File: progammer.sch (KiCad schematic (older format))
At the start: 10 parts, among them J5 USB_B_Micro, U1 ICE40HX4K-TQ144, U3 93LCxxBT-I_OT, U4 FT2232H, U5 IS25LP080D

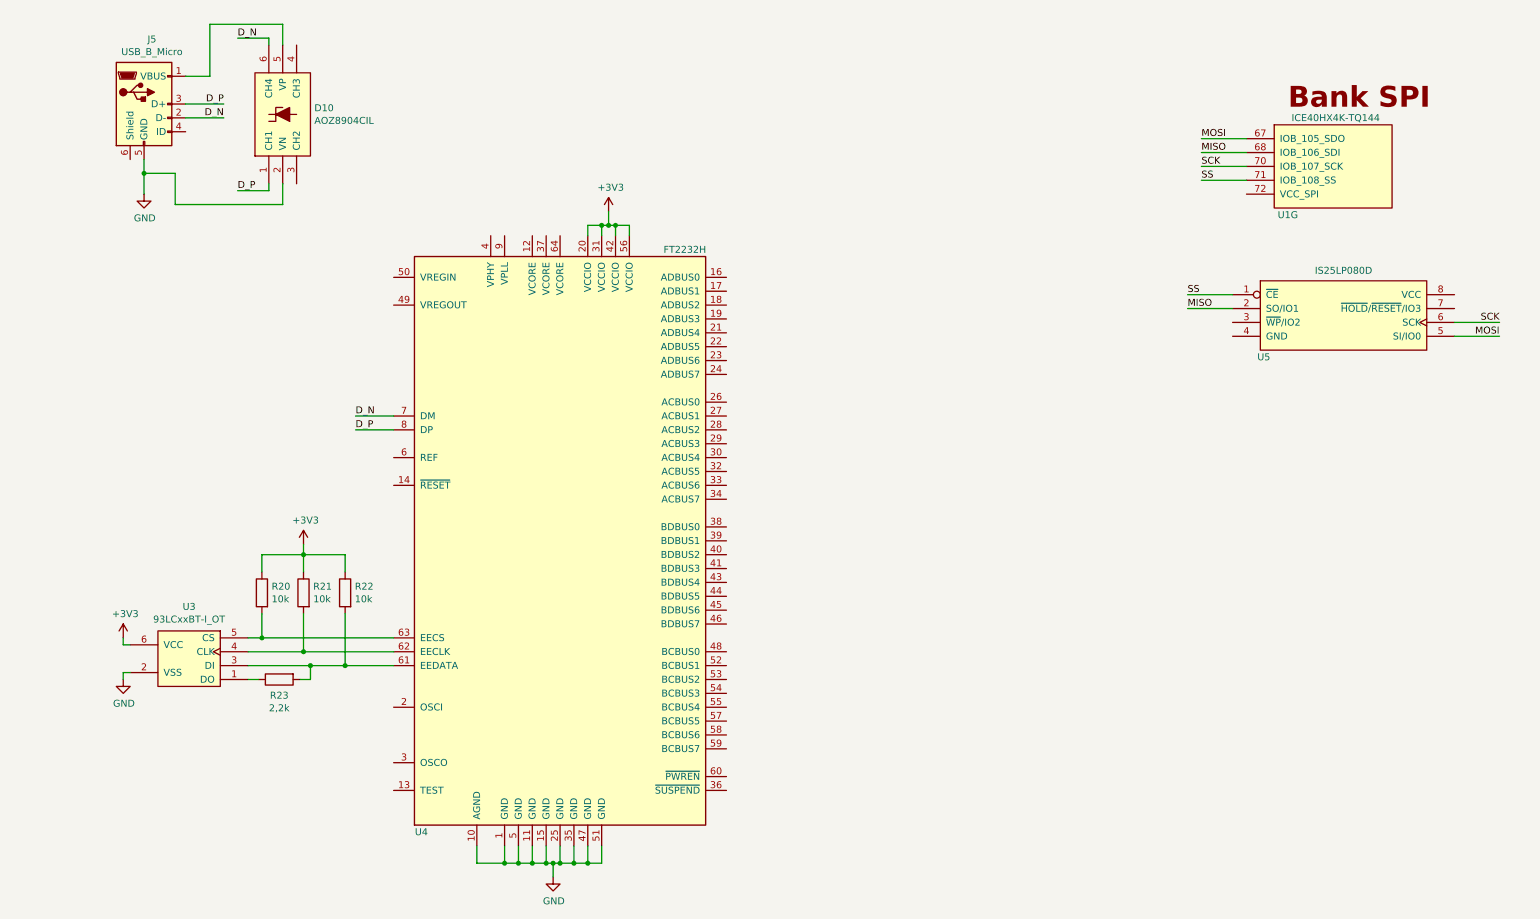
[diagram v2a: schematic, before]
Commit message: Progress on FTDI - added Oscillator and 1.8 V supply
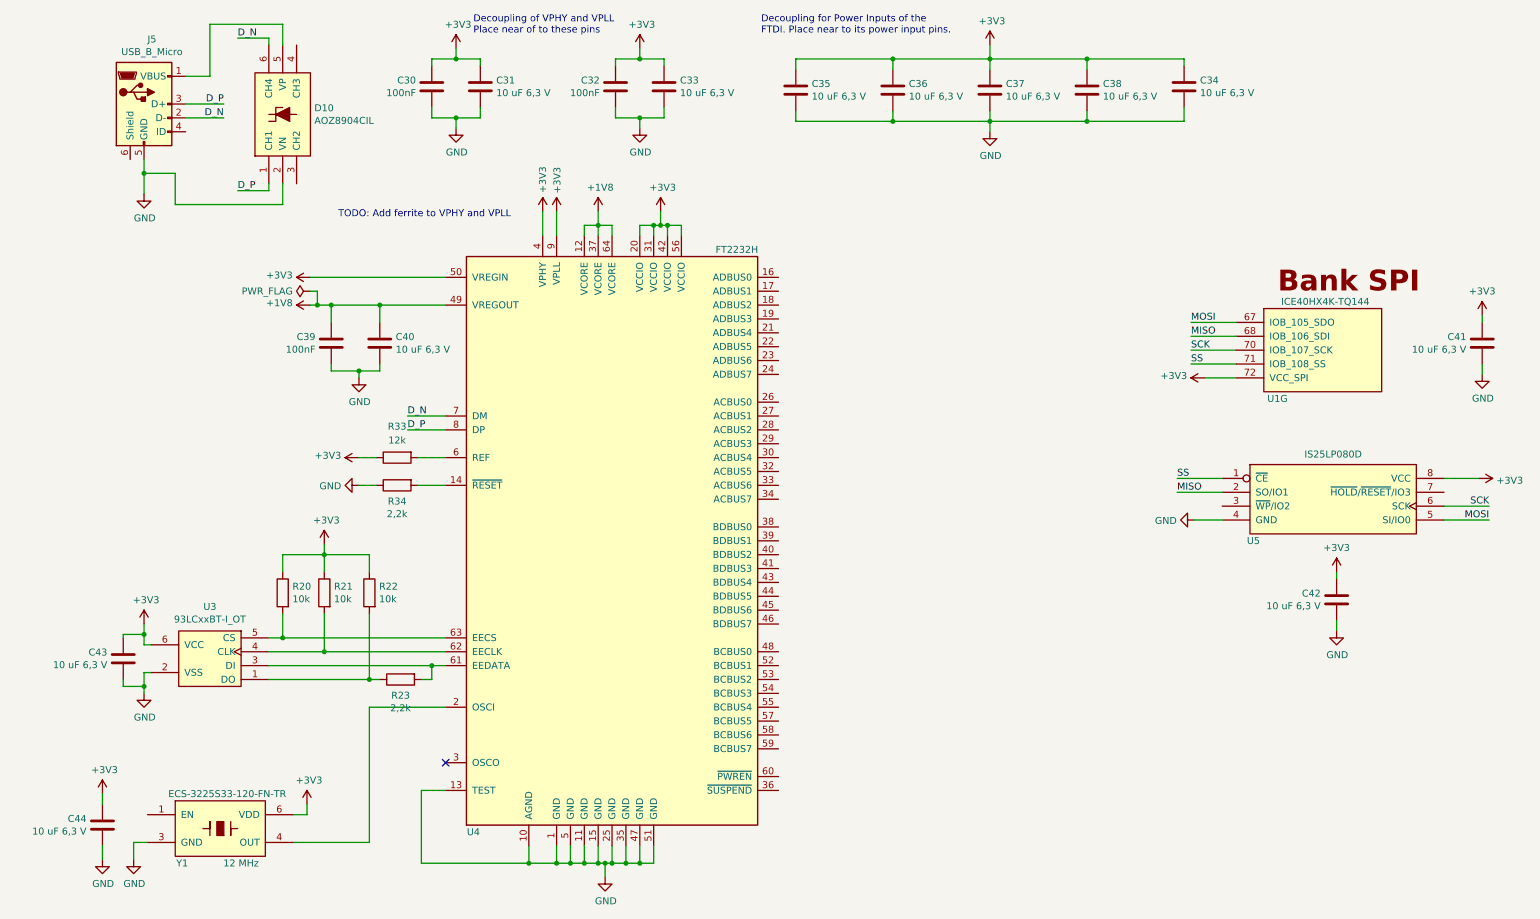
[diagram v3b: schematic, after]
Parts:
- added C30, C32, C39: 100nF, Capacitor_SMD:C_0603_1608Metric, symbol Device:C
- added C31, C33, C34, C35, C36, C37, C38, C40, C41, C42, C43, C44: 10 uF 6,3 V, Capacitor_SMD:C_0603_1608Metric, symbol Device:C
- added R33: 12k, Resistor_SMD:R_0603_1608Metric, symbol Device:R
- added R34: 2,2k, Resistor_SMD:R_0603_1608Metric, symbol Device:R
- added Y1: ECS-3225S33-120-FN-TR, footprints:ECS-3225S_3.2x2.5mm_footprint, symbol ECS-3225S:ECS-3225S33
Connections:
- net +3V3: now also U1.72 (VCC_SPI), U4.4 (VPHY), U4.50 (VREGIN), U4.9 (VPLL), U5.8 (VCC), C30.1, C31.1, C32.1, C33.1, C34.1, C35.1, C36.1, C37.1, C38.1, C41.1, C42.1, C43.1, C44.1, R33.1, Y1.6 (VDD)
- net GND: now also U4.13 (TEST), U5.4 (GND), C30.2, C31.2, C32.2, C33.2, C34.2, C35.2, C36.2, C37.2, C38.2, C39.2, C40.2, C41.2, C42.2, C43.2, C44.2, R34.1, Y1.3 (GND)
- net +1V8: now reaches U4.12 (VCORE)
- net +1V8: now also U4.37 (VCORE), U4.49 (VREGOUT), U4.64 (VCORE), C39.1, C40.1
- net at U4.14 (~RESET): now also R34.2
- net at U4.2 (OSCI): now also Y1.4 (OUT)
- net at U4.6 (REF): now also R33.2
- net at R23.2, U3.3 (DI), U4.61 (EEDATA): no longer R22.2
- net at R23.1, U3.1 (DO): now also R22.2
- no-connect marks 0 -> 1
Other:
- note added: "Decoupling for Power Inputs of the\nFTDI. Place near to its power input pins."
- note added: "Decoupling of VPHY and VPLL\nPlace near of to these pins"
- note added: "TODO: Add ferrite to VPHY and VPLL"
- moved on the sheet: R20, R21, R22, R23, U1G, U3, U4, U5

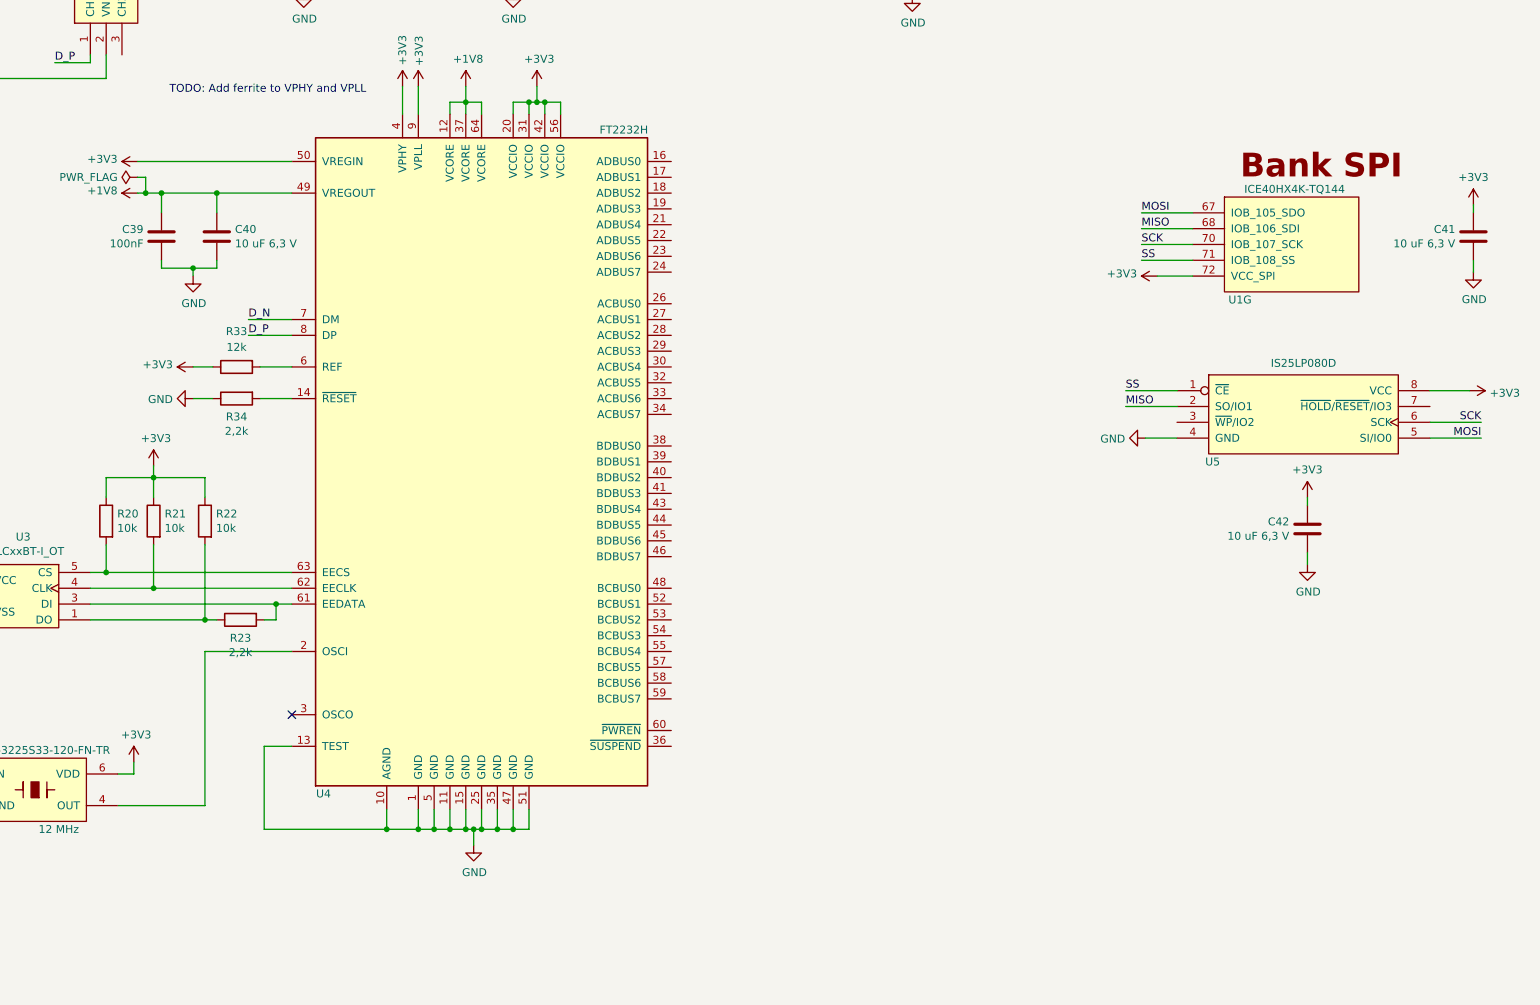
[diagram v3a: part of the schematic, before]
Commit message: Continued on Programmer, moved the header signals around the package to free some space for a fully featured UART/RS232(TTL)
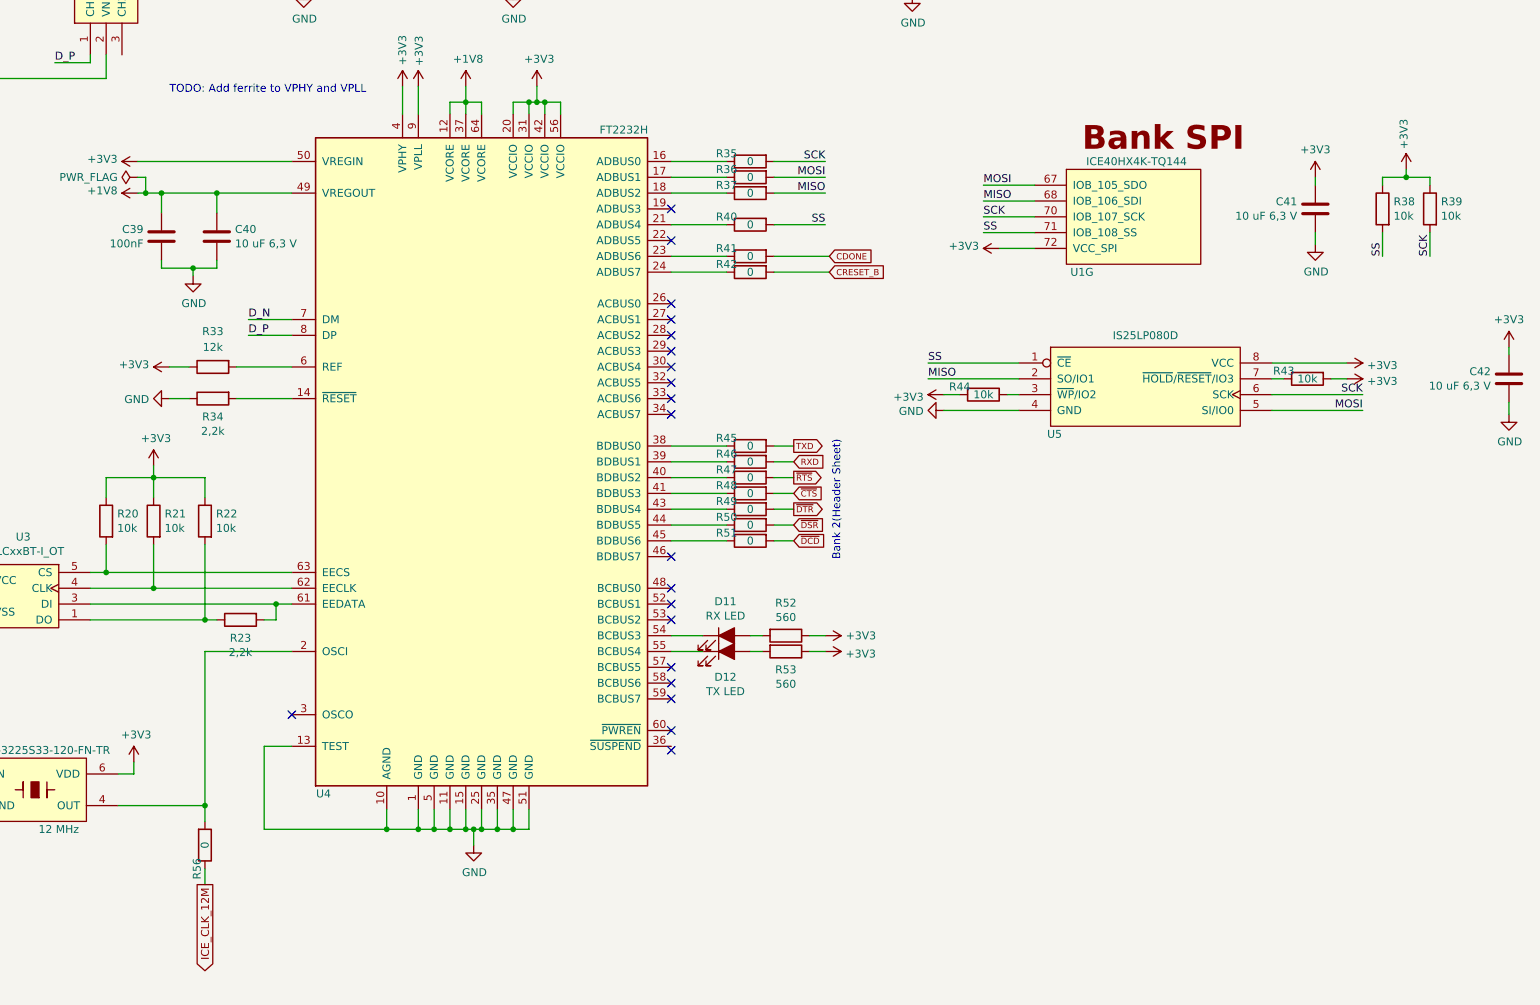
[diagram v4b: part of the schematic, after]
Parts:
- added D11: RX LED, LED_SMD:LED_0603_1608Metric, symbol Device:LED_ALT
- added D12: TX LED, LED_SMD:LED_0603_1608Metric, symbol Device:LED_ALT
- added R35, R36, R37, R40, R41, R42, R45, R46, R47, R48, R49, R50, R51, R56: 0, Resistor_SMD:R_0603_1608Metric, symbol Device:R
- added R38, R39, R43, R44: 10k, Resistor_SMD:R_0603_1608Metric, symbol Device:R
- added R52, R53: 560, Resistor_SMD:R_0603_1608Metric, symbol Device:R
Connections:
- net +3V3: now also R38.1, R39.1, R43.2, R44.2, R52.1, R53.1
- net MISO: now also R37.2
- net MOSI: now also R36.2
- net SCK: now also R35.2, R39.2
- net SS: now also R38.2, R40.2
- net at U4.16 (ADBUS0): now also R35.1
- net at U4.17 (ADBUS1): now also R36.1
- net at U4.18 (ADBUS2): now also R37.1
- net at U4.2 (OSCI), Y1.4 (OUT): now also R56.2
- net at U4.21 (ADBUS4): now also R40.1
- net at U4.23 (ADBUS6): now also R41.1
- net at U4.24 (ADBUS7): now also R42.1
- net at U4.38 (BDBUS0): now also R45.1
- net at U4.39 (BDBUS1): now also R46.1
- net at U4.40 (BDBUS2): now also R47.1
- net at U4.41 (BDBUS3): now also R48.1
- net at U4.43 (BDBUS4): now also R49.1
- net at U4.44 (BDBUS5): now also R50.1
- net at U4.45 (BDBUS6): now also R51.1
- net at U4.54 (BCBUS3): now also D11.1 (K)
- net at U4.55 (BCBUS4): now also D12.1 (K)
- net at U5.3 (~WP~/IO2): now also R44.1
- net at U5.7 (~HOLD~/~RESET~/IO3): now also R43.1
- new net: D11.2 (A), R52.2
- new net: D12.2 (A), R53.2
- new net CDONE: R41.2
- new net CRESET_B: R42.2
- new net ICE_CLK_12M: R56.1
- new net RXD: R46.2
- new net TXD: R45.2
- new net ~CTS~: R48.2
- new net ~DCD~: R51.2
- new net ~DSR~: R50.2
- new net ~DTR~: R49.2
- new net ~RTS~: R47.2
- no-connect marks 1 -> 20
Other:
- note added: "Bank 2(Header Sheet)"
- moved on the sheet: C41, C42, R33, R34, U1G, U5

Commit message: Added switches, added 5 V rail and 17 V input(with filtering). Power is mostly done.
Also added a first version of buffers to ftdi chip. I'll change the evtl.

Started to route power section.
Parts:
- removed C34, C35, C36, C37, C38, C41, C42, C43, C44: 10 uF 6,3 V, Capacitor_SMD:C_0603_1608Metric, symbol Device:C
- removed R35, R40, R41, R42, R46, R47, R48, R49, R50, R51, R56: 0, Resistor_SMD:R_0603_1608Metric, symbol Device:R
- added C46, C47: 1 uF 16 V, Capacitor_SMD:C_0603_1608Metric, symbol Device:C
- added C54, C55, C65: 10 uF 6,3 V, Capacitor_SMD:C_0603_1608Metric, symbol Device:C
- added C56, C57, C58, C59, C60, C61, C62, C63, C64, C66, C67, C68, C69, C70, C71, C72: 100nF, Capacitor_SMD:C_0603_1608Metric, symbol Device:C
- added FB3, FB4, FB5, FB6: 330 Ohm, Resistor_SMD:R_0805_2012Metric, symbol Device:Ferrite_Bead_Small
- added U11, U13: TXS0108EPW, Package_SO:TSSOP-20_4.4x6.5mm_P0.65mm, symbol Logic_LevelTranslator:TXS0108EPW
- added U14: MIC5365-3.3YC5, Package_TO_SOT_SMD:SOT-353_SC-70-5, symbol Regulator_Linear:MIC5365-3.3YC5
- R36: value 0 -> 4k7
- R37, R45: value 0 -> 10k
- Y1: f 12 MHz -> 12 MHz <=30 ppm
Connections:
- net +1V8: now also C61.1, C62.1, C63.1
- net +3V3: now also C64.1, C65.1, C68.1, C69.1, C70.1, U11.19 (VCCB), U13.19 (VCCB); no longer C30.1, C31.1, C32.1, C33.1, R20.1, R21.1, R22.1, R33.1, R52.1, R53.1, U3.6 (VCC), U4.20 (VCCIO), U4.31 (VCCIO), U4.4 (VPHY), U4.42 (VCCIO), U4.50 (VREGIN), U4.56 (VCCIO), U4.9 (VPLL), Y1.6 (VDD)
- net CDONE: now also U11.15 (B5)
- net CRESET_B: now also U11.14 (B6)
- net D_N: now also D10.1 (CH1), J5.3 (D+); no longer D10.6 (CH4), J5.2 (D-)
- net D_P: now also D10.6 (CH4), J5.2 (D-); no longer D10.1 (CH1), J5.3 (D+)
- net GND: now also R33.1, R37.2, R45.2, C46.2, C47.2, C55.2, C56.2, C57.2, C58.2, C59.2, C60.2, C61.2, C62.2, C63.2, C64.2, C65.2, C66.2, C67.2, C68.2, C69.2, C70.2, C71.2, C72.2, FB6.1, U11.11 (GND), U13.11 (GND), U14.2 (GND); no longer D10.2 (VN), J5.5 (GND), R34.1
- net ICE_CLK_12M: now also U13.12 (B8)
- net MISO: now also U11.17 (B3); no longer R37.2
- net MOSI: now also U11.18 (B2); no longer R36.2
- net RXD: now also U11.12 (B8)
- net SCK: now also U11.20 (B1)
- net SS: now also U11.16 (B4)
- net TXD: now also U11.13 (B7); no longer R45.2
- net ~CTS~: now also U13.18 (B2)
- net ~DCD~: now also U13.15 (B5)
- net ~DSR~: now also U13.16 (B4)
- net ~DTR~: now also U13.17 (B3)
- net ~RTS~: now also U13.20 (B1)
- net at U4.16 (ADBUS0): now also U11.1 (A1)
- net at U4.17 (ADBUS1): now also U11.3 (A2); no longer R36.1
- net at U4.18 (ADBUS2): now also U11.4 (A3); no longer R37.1
- net 12_MHZ: now reaches U4.2 (OSCI), Y1.4 (OUT)
- net 12_MHZ: now also U13.9 (A8)
- net at U4.21 (ADBUS4): now also U11.5 (A4)
- net at U4.23 (ADBUS6): now also U11.6 (A5)
- net at U4.24 (ADBUS7): now also U11.7 (A6)
- net at U4.38 (BDBUS0): now also U11.8 (A7); no longer R45.1
- net at U4.39 (BDBUS1): now also U11.9 (A8)
- net at U4.40 (BDBUS2): now also U13.1 (A1)
- net at U4.41 (BDBUS3): now also U13.3 (A2)
- net at U4.43 (BDBUS4): now also U13.4 (A3)
- net at U4.44 (BDBUS5): now also U13.5 (A4)
- net at U4.45 (BDBUS6): now also U13.6 (A5)
- net at U4.59 (BCBUS7): now also R36.2, R37.1
- net VBUS_IN: now reaches D10.5 (VP), J5.1 (VBUS)
- net VBUS_IN: now also C54.1, FB3.2
- net at J5.6 (Shield): now also R45.1
- net +3V3_FTDI: now reaches Y1.1 (EN)
- net +3V3_FTDI: now also R20.1, R21.1, R22.1, R34.1, R52.1, R53.1, U3.6 (VCC), U4.20 (VCCIO), U4.31 (VCCIO), U4.42 (VCCIO), U4.50 (VREGIN), U4.56 (VCCIO), Y1.6 (VDD), C47.1, C55.1, C56.1, C57.1, C58.1, C59.1, C60.1, C66.1, C67.1, C71.1, C72.1, FB4.2, FB5.2, U11.10 (OE), U11.2 (VCCA), U13.10 (OE), U13.2 (VCCA), U14.5 (VOUT)
- new net GNDBUS: C54.2, D10.2 (VN), FB6.2, J5.5 (GND)
- new net VBUS: C46.1, FB3.1, R36.1, U14.1 (VIN), U14.3 (EN)
- new net V_USB_PHY: C32.1, C33.1, FB4.1, U4.4 (VPHY)
- new net V_USB_PLL: C30.1, C31.1, FB5.1, U4.9 (VPLL)
- no-connect marks 20 -> 27
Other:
- note added: "Decoupling for SPI Bank"
- note added: "Decoupling for buffers"
- note removed: "TODO: Add ferrite to VPHY and VPLL"
- moved on the sheet: C30, C31, C32, C33, C39, C40, D10, D11, D12, J5, R20, R21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
